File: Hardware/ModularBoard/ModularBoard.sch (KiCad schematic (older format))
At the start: 2 parts

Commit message: Complete board with just MCU and USB port
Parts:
- removed CON?: USB-MINI-B, symbol USB-MINI-B
- added X1: USB-MB-S, con-usb-USB-MB-S, symbol USB-MB-S
- gave numbers to parts that had none: 1
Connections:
- wire segments 4 -> 8
- no-connect marks 0 -> 8
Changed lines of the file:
@@
 LIBS:contrib
 LIBS:valves
+LIBS:con-usb
 LIBS:ModularBoard-cache
 EELAYER 27 0
@@
 $EndDescr
 $Comp
-L ATTINY85-P IC?
+L ATTINY85-P IC1
 U 1 1 520B10CA
 P 5900 4150
-F 0 "IC?" H 4850 4550 60  0000 C CNN
+F 0 "IC1" H 4850 4550 60  0000 C CNN
 F 1 "ATTINY85-P" H 6750 3750 60  0000 C CNN
 F 2 "DIP8" H 4850 3750 60  0001 C CNN
@@
 $EndComp
 $Comp
-L +5V #PWR?
+L +5V #PWR01
 U 1 1 520B11FD
 P 7400 3750
-F 0 "#PWR?" H 7400 3840 20  0001 C CNN
+F 0 "#PWR01" H 7400 3840 20  0001 C CNN
 F 1 "+5V" H 7400 3840 30  0000 C CNN
 F 2 "" H 7400 3750 60  0000 C CNN
@@
 	7400 3900 7400 3750
 $Comp
-L GND #PWR?
+L GND #PWR02
 U 1 1 520B1251
 P 7400 4550
-F 0 "#PWR?" H 7400 4550 30  0001 C CNN
+F 0 "#PWR02" H 7400 4550 30  0001 C CNN
 F 1 "GND" H 7400 4480 30  0001 C CNN
 F 2 "" H 7400 4550 60  0000 C CNN
@@
 	7400 4400 7250 4400
 $Comp
-L USB-MINI-B CON?
-U 1 1 520B13E0
-P 9500 4350
-F 0 "CON?" H 9250 4800 60  0000 C CNN
-F 1 "USB-MINI-B" H 9450 3850 60  0000 C CNN
-F 2 "" H 9500 4350 60  0000 C CNN
-F 3 "" H 9500 4350 60  0000 C CNN
-	1    9500 4350
+L USB-MB-S X1
+U 1 1 520B1891
+P 9150 4250
+F 0 "X1" H 9150 4250 50  0000 C CNN
+F 1 "USB-MB-S" H 9150 4250 50  0000 C CNN
+F 2 "con-usb-USB-MB-S" H 9150 4400 50  0001 C CNN
+F 3 "" H 9150 4250 60  0000 C CNN
+	1    9150 4250
 	1    0    0    -1
 $EndComp
+$Comp
+L +5V #PWR03
+U 1 1 520B18BF
+P 8900 3800
+F 0 "#PWR03" H 8900 3890 20  0001 C CNN
+F 1 "+5V" H 8900 3890 30  0000 C CNN
+F 2 "" H 8900 3800 60  0000 C CNN
+F 3 "" H 8900 3800 60  0000 C CNN
+	1    8900 3800
+	1    0    0    -1
+$EndComp
+$Comp
+L GND #PWR04
+U 1 1 520B18D4
+P 8900 4400
+F 0 "#PWR04" H 8900 4400 30  0001 C CNN
+F 1 "GND" H 8900 4330 30  0001 C CNN
+F 2 "" H 8900 4400 60  0000 C CNN
+F 3 "" H 8900 4400 60  0000 C CNN
+	1    8900 4400
+	1    0    0    -1
+$EndComp
+Wire Wire Line
+	8900 3800 8900 3950
+Wire Wire Line
+	8900 3950 9050 3950
+Wire Wire Line
+	8900 4400 8900 4250
+Wire Wire Line
+	8900 4250 9050 4250
+NoConn ~ 9050 4050
+NoConn ~ 9050 4150
+NoConn ~ 4550 3900
+NoConn ~ 4550 4000
+NoConn ~ 4550 4100
+NoConn ~ 4550 4200
+NoConn ~ 4550 4300
+NoConn ~ 4550 4400
 $EndSCHEMATC

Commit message: Fixed derpy USB port, now micro instead of mini
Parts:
- removed X1: USB-MB-S, con-usb-USB-MB-S, symbol USB-MB-S
- added J1: GSG-USB-MICRO-B, symbol GSG-USB-MICRO-B
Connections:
- no-connect marks 8 -> 9
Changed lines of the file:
@@
 LIBS:valves
 LIBS:con-usb
+LIBS:hackrf
 LIBS:ModularBoard-cache
 EELAYER 27 0
@@
 	7400 4400 7250 4400
 $Comp
-L USB-MB-S X1
-U 1 1 520B1891
-P 9150 4250
-F 0 "X1" H 9150 4250 50  0000 C CNN
-F 1 "USB-MB-S" H 9150 4250 50  0000 C CNN
-F 2 "con-usb-USB-MB-S" H 9150 4400 50  0001 C CNN
-F 3 "" H 9150 4250 60  0000 C CNN
-	1    9150 4250
-	1    0    0    -1
-$EndComp
-$Comp
 L +5V #PWR03
 U 1 1 520B18BF
@@
 L GND #PWR04
 U 1 1 520B18D4
-P 8900 4400
-F 0 "#PWR04" H 8900 4400 30  0001 C CNN
-F 1 "GND" H 8900 4330 30  0001 C CNN
-F 2 "" H 8900 4400 60  0000 C CNN
-F 3 "" H 8900 4400 60  0000 C CNN
-	1    8900 4400
+P 8900 4500
+F 0 "#PWR04" H 8900 4500 30  0001 C CNN
+F 1 "GND" H 8900 4430 30  0001 C CNN
+F 2 "" H 8900 4500 60  0000 C CNN
+F 3 "" H 8900 4500 60  0000 C CNN
+	1    8900 4500
 	1    0    0    -1
 $EndComp
 Wire Wire Line
 	8900 3800 8900 3950
-Wire Wire Line
-	8900 3950 9050 3950
-Wire Wire Line
-	8900 4400 8900 4250
-Wire Wire Line
-	8900 4250 9050 4250
-NoConn ~ 9050 4050
-NoConn ~ 9050 4150
 NoConn ~ 4550 3900
 NoConn ~ 4550 4000
@@
 NoConn ~ 4550 4300
 NoConn ~ 4550 4400
+$Comp
+L GSG-USB-MICRO-B J1
+U 1 1 520B2785
+P 9300 4150
+F 0 "J1" H 9300 4450 60  0000 C CNN
+F 1 "GSG-USB-MICRO-B" H 9300 3800 60  0000 C CNN
+F 2 "" H 9300 4150 60  0000 C CNN
+F 3 "" H 9300 4150 60  0000 C CNN
+	1    9300 4150
+	1    0    0    -1
+$EndComp
+Wire Wire Line
+	8900 3950 9050 3950
+Wire Wire Line
+	8900 4500 8900 4350
+Wire Wire Line
+	8900 4350 9050 4350
+NoConn ~ 9050 4050
+NoConn ~ 9050 4150
+NoConn ~ 9050 4250
 $EndSCHEMATC

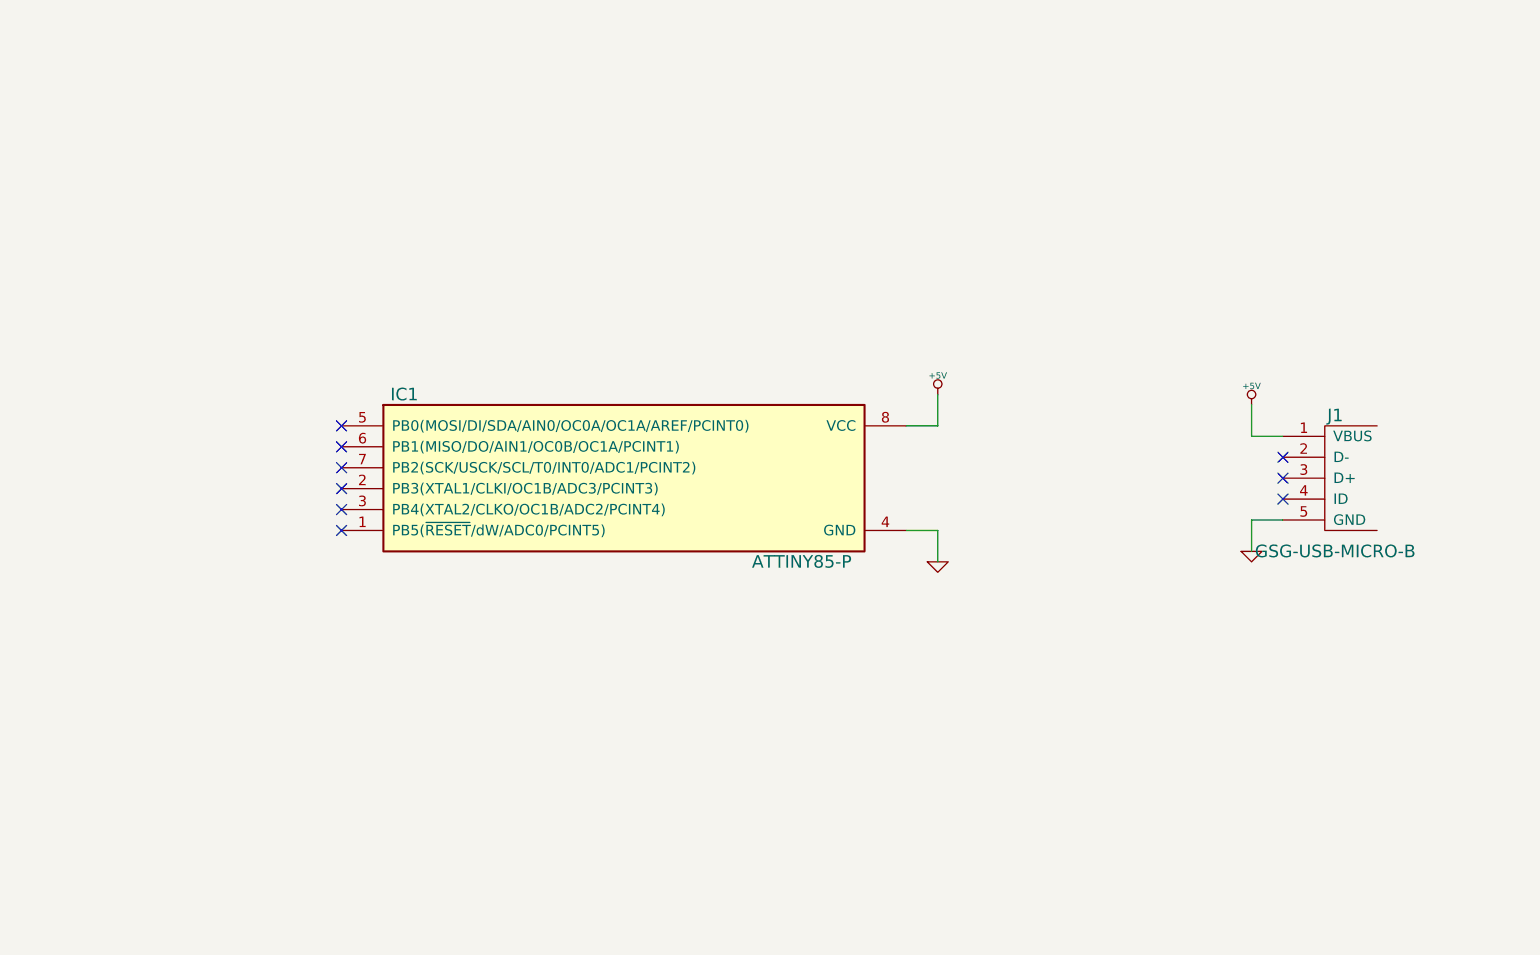
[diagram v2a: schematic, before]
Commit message: Updated schematic, should just need a few more breakout pins, maybe caps for filtering
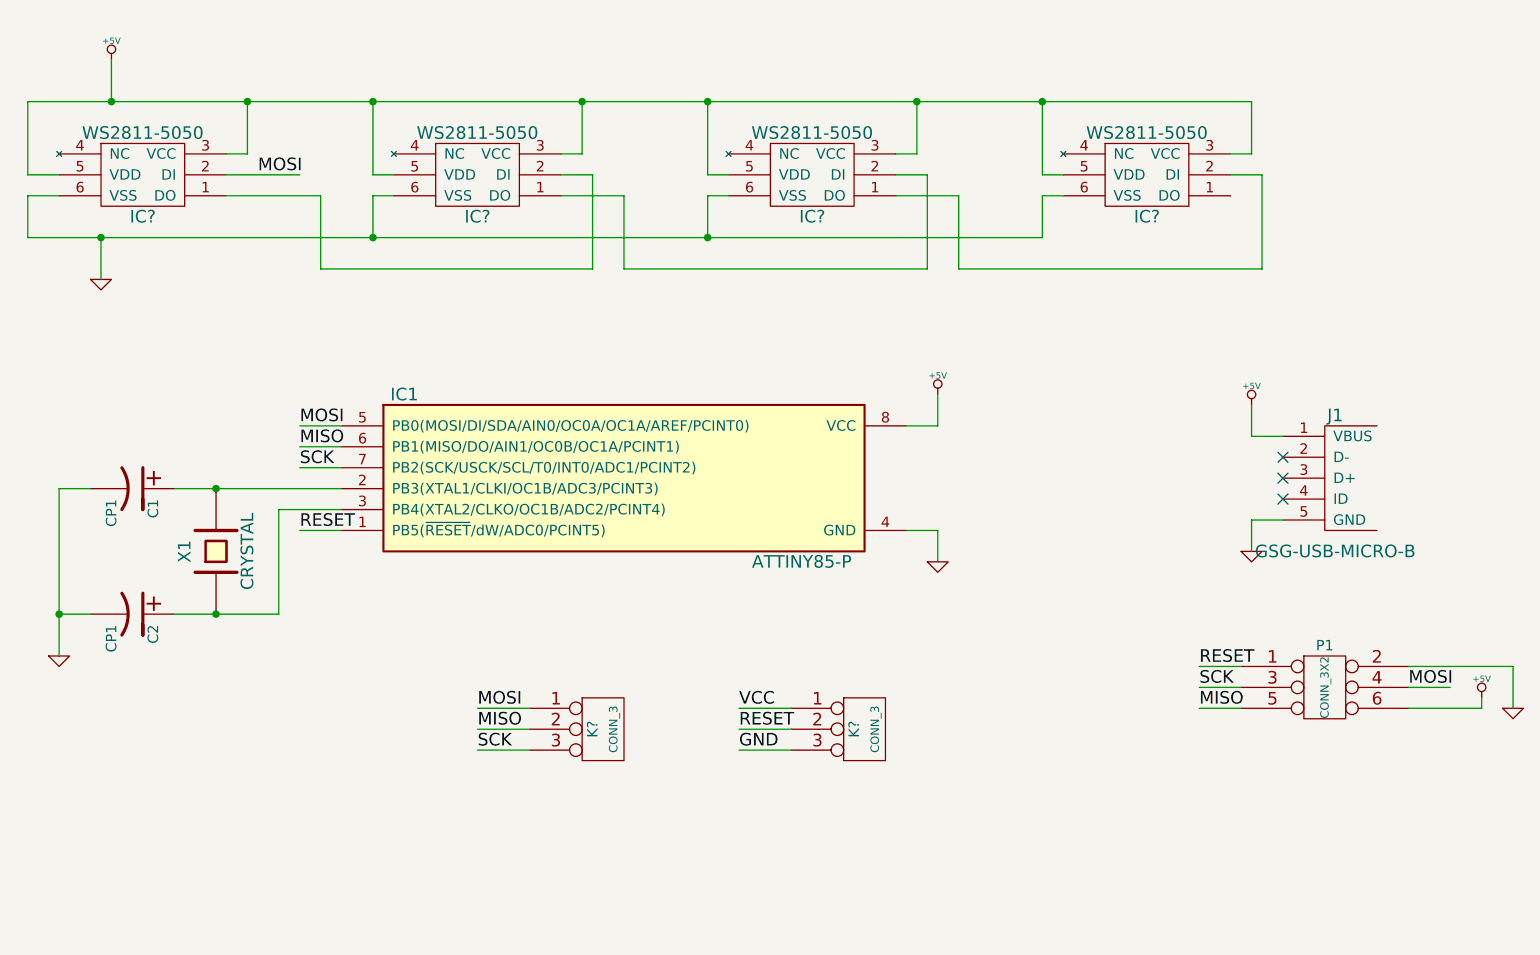
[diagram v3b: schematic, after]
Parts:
- added C1, C2: CP1, ~, symbol CP1
- added IC? (x4): WS2811-5050, symbol WS2811-5050
- added K? (x2): CONN_3, symbol CONN_3
- added P1: CONN_3X2, symbol CONN_3X2
- added X1: CRYSTAL, ~, symbol CRYSTAL
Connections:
- net +5V: now also IC?.3 (VCC), IC?.3 (VCC), IC?.3 (VCC), IC?.3 (VCC), IC?.5 (VDD), IC?.5 (VDD), IC?.5 (VDD), IC?.5 (VDD), P1.6
- net GND: now also C1.2, C2.2, IC?.6 (VSS), IC?.6 (VSS), IC?.6 (VSS), IC?.6 (VSS), K?.3 (P3), P1.2
- net RESET: now reaches IC1.1 (PB5(~RESET~/dW/ADC0/PCINT5))
- net RESET: now also K?.2 (PM), P1.1
- net at IC1.2 (PB3(XTAL1/CLKI/OC1B/ADC3/PCINT3)): now also C1.1, X1.2
- net at IC1.3 (PB4(XTAL2/CLKO/OC1B/ADC2/PCINT4)): now also C2.1, X1.1
- net MOSI: now reaches IC1.5 (PB0(MOSI/DI/SDA/AIN0/OC0A/OC1A/AREF/PCINT0))
- net MOSI: now also IC?.2 (DI), K?.1 (P1), P1.4
- net MISO: now reaches IC1.6 (PB1(MISO/DO/AIN1/OC0B/OC1A/PCINT1))
- net MISO: now also K?.2 (PM), P1.5
- net SCK: now reaches IC1.7 (PB2(SCK/USCK/SCL/T0/INT0/ADC1/PCINT2))
- net SCK: now also K?.3 (P3), P1.3
- new net: IC?.1 (DO), IC?.2 (DI) (x3)
- new net VCC: K?.1 (P1)
- no-connect marks 9 -> 3

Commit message: Schematic should be done, board partially implemented
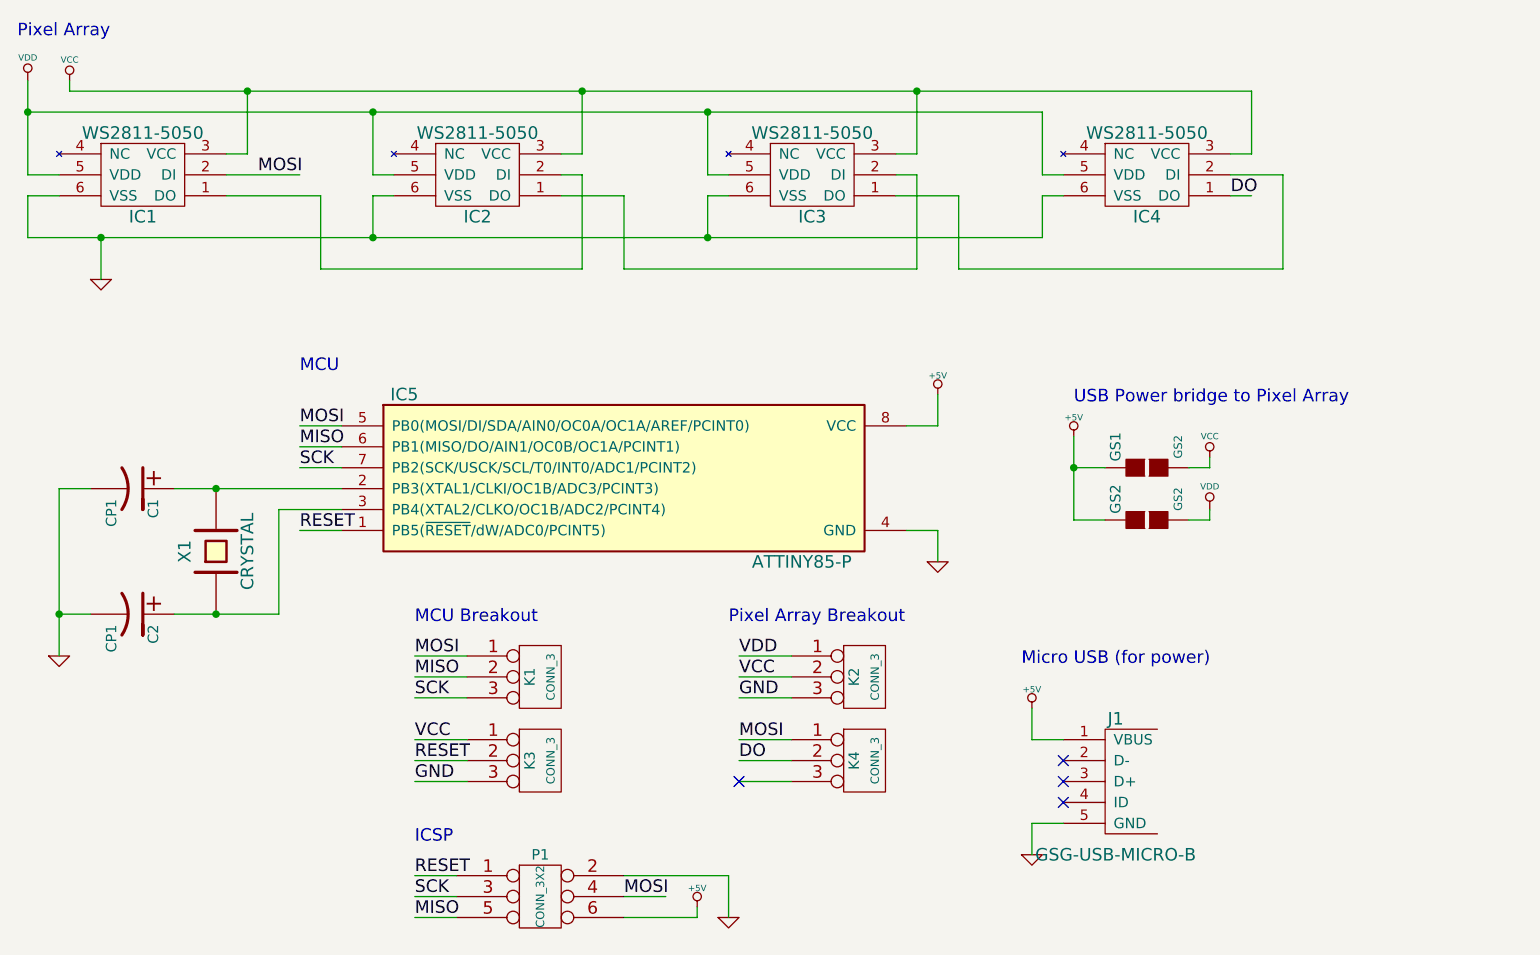
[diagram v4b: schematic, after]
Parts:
- added GS1, GS2: GS2, symbol GS2
- added K2, K4: CONN_3, symbol CONN_3
- gave numbers to parts that had none: 6
- renumbered IC1 to IC5
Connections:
- net labels added: DO, VDD
- wire segments 77 -> 92
- no-connect marks 3 -> 4
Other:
- note added: "ICSP"
- note added: "MCU"
- note added: "MCU Breakout"
- note added: "Micro USB (for power)"
- note added: "Pixel Array"
- note added: "Pixel Array Breakout"
- note added: "USB Power bridge to Pixel Array"
- moved on the sheet: J1, K1, K3, P1

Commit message: board should be done, save trace width tweaking
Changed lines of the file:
@@
 Wire Wire Line
 	5150 5600 4900 5600
-Text Label 4900 5400 0    60   ~ 0
-VCC
 Text Label 4900 5600 0    60   ~ 0
 GND
@@
 Text Label 6450 5100 0    60   ~ 0
 VCC
+$Comp
+L +5V #PWR?
+U 1 1 520F1FA0
+P 4900 5400
+F 0 "#PWR?" H 4900 5490 20  0001 C CNN
+F 1 "+5V" H 4900 5490 30  0000 C CNN
+F 2 "" H 4900 5400 60  0000 C CNN
+F 3 "" H 4900 5400 60  0000 C CNN
+	1    4900 5400
+	1    0    0    -1
+$EndComp
 $EndSCHEMATC

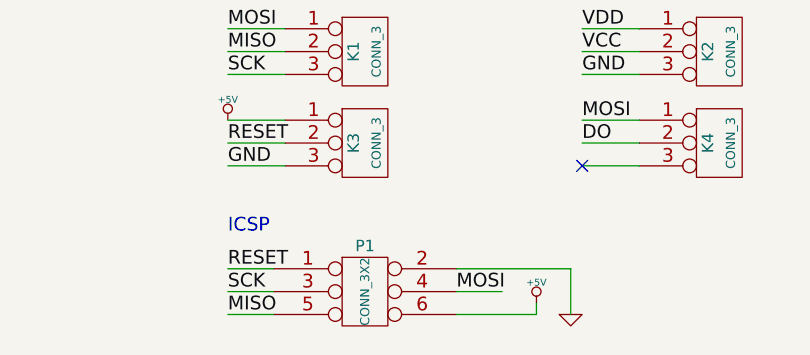
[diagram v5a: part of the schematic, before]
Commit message: Fixed ICSP header
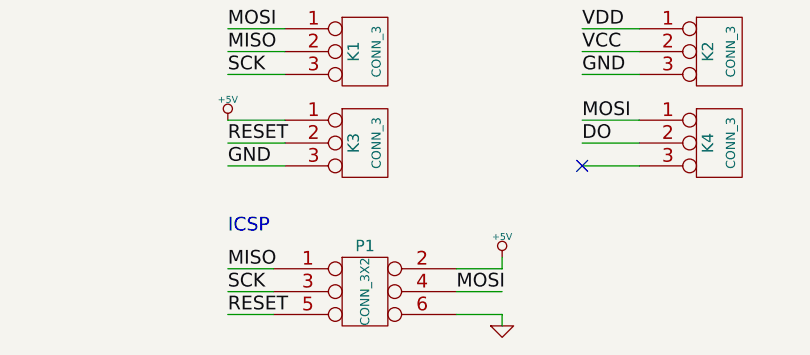
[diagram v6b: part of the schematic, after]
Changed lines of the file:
@@
 Sheet 1 1
 Title ""
-Date "17 aug 2013"
+Date "18 aug 2013"
 Rev ""
 Comp ""
@@
 L +5V #PWR06
 U 1 1 520C3AF8
-P 6250 6200
-F 0 "#PWR06" H 6250 6290 20  0001 C CNN
-F 1 "+5V" H 6250 6290 30  0000 C CNN
-F 2 "" H 6250 6200 60  0000 C CNN
-F 3 "" H 6250 6200 60  0000 C CNN
-	1    6250 6200
+P 6100 6000
+F 0 "#PWR06" H 6100 6090 20  0001 C CNN
+F 1 "+5V" H 6100 6090 30  0000 C CNN
+F 2 "" H 6100 6000 60  0000 C CNN
+F 3 "" H 6100 6000 60  0000 C CNN
+	1    6100 6000
 	1    0    0    -1
 $EndComp
@@
 L GND #PWR07
 U 1 1 520C3B1A
-P 6400 6250
-F 0 "#PWR07" H 6400 6250 30  0001 C CNN
-F 1 "GND" H 6400 6180 30  0001 C CNN
-F 2 "" H 6400 6250 60  0000 C CNN
-F 3 "" H 6400 6250 60  0000 C CNN
-	1    6400 6250
-	1    0    0    -1
-$EndComp
-Wire Wire Line
-	5900 6050 6400 6050
+P 6100 6300
+F 0 "#PWR07" H 6100 6300 30  0001 C CNN
+F 1 "GND" H 6100 6230 30  0001 C CNN
+F 2 "" H 6100 6300 60  0000 C CNN
+F 3 "" H 6100 6300 60  0000 C CNN
+	1    6100 6300
+	1    0    0    -1
+$EndComp
 Text Label 4350 4400 0    60   ~ 0
 RESET
@@
 Wire Wire Line
 	4900 6050 5100 6050
-Text Label 4900 6050 0    60   ~ 0
-RESET
 Wire Wire Line
 	4550 3900 4350 3900
@@
 Wire Wire Line
 	5100 6250 4900 6250
-Text Label 4900 6250 0    60   ~ 0
-MISO
 Wire Wire Line
 	5100 6150 4900 6150
@@
 Text Label 4350 4100 0    60   ~ 0
 SCK
-Wire Wire Line
-	6400 6050 6400 6250
-Wire Wire Line
-	5900 6250 6250 6250
-Wire Wire Line
-	6250 6250 6250 6200
 $Comp
 L WS2811-5050 IC1
@@
 	1    0    0    -1
 $EndComp
+Wire Wire Line
+	5900 6250 6100 6250
+Wire Wire Line
+	6100 6250 6100 6300
+Wire Wire Line
+	5900 6050 6100 6050
+Wire Wire Line
+	6100 6050 6100 6000
+Text Label 4900 6050 0    60   ~ 0
+MISO
+Text Label 4900 6250 0    60   ~ 0
+RESET
 $EndSCHEMATC

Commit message: Its compact! Fits in 5x5cm square
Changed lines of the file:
@@
 Text Label 4900 5500 0    60   ~ 0
 RESET
-Text Label 4900 5000 0    60   ~ 0
-MOSI
 Text Label 4900 5100 0    60   ~ 0
 MISO
-Text Label 4900 5200 0    60   ~ 0
-SCK
 $Comp
 L VDD #PWR09
@@
 Text Label 4900 6250 0    60   ~ 0
 RESET
+Text Label 4900 5200 0    60   ~ 0
+MOSI
+Text Label 4900 5000 0    60   ~ 0
+SCK
 $EndSCHEMATC
